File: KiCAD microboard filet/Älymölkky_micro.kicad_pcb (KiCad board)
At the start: 2 copper layers, 84 parts, among them U1 nRF52810-QCxx, X1 32MHz Crystal, X1_C1 12pF, X1_C2 12pF, X2 32.768 kHz Crystal, X2_C11 12pF, X2_C12 12pF

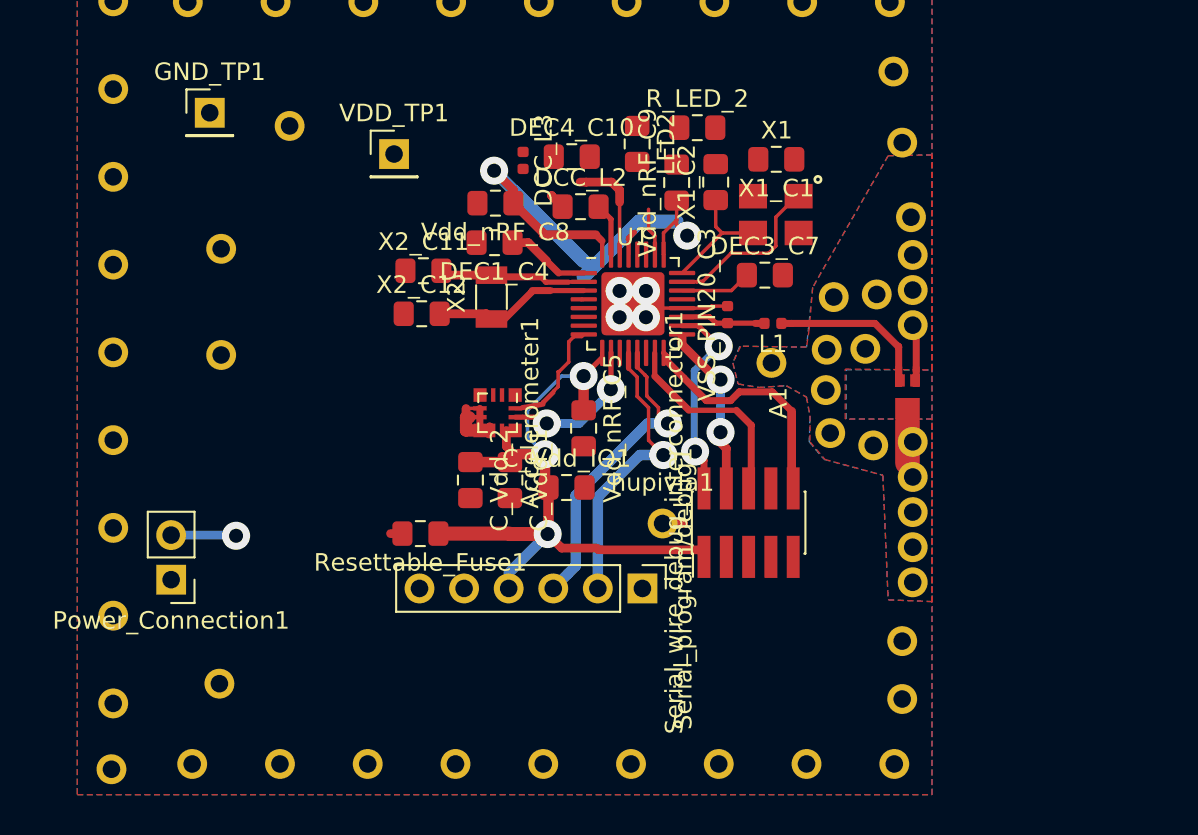
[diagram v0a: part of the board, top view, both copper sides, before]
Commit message: Changed programming interface to standalone pinheaders
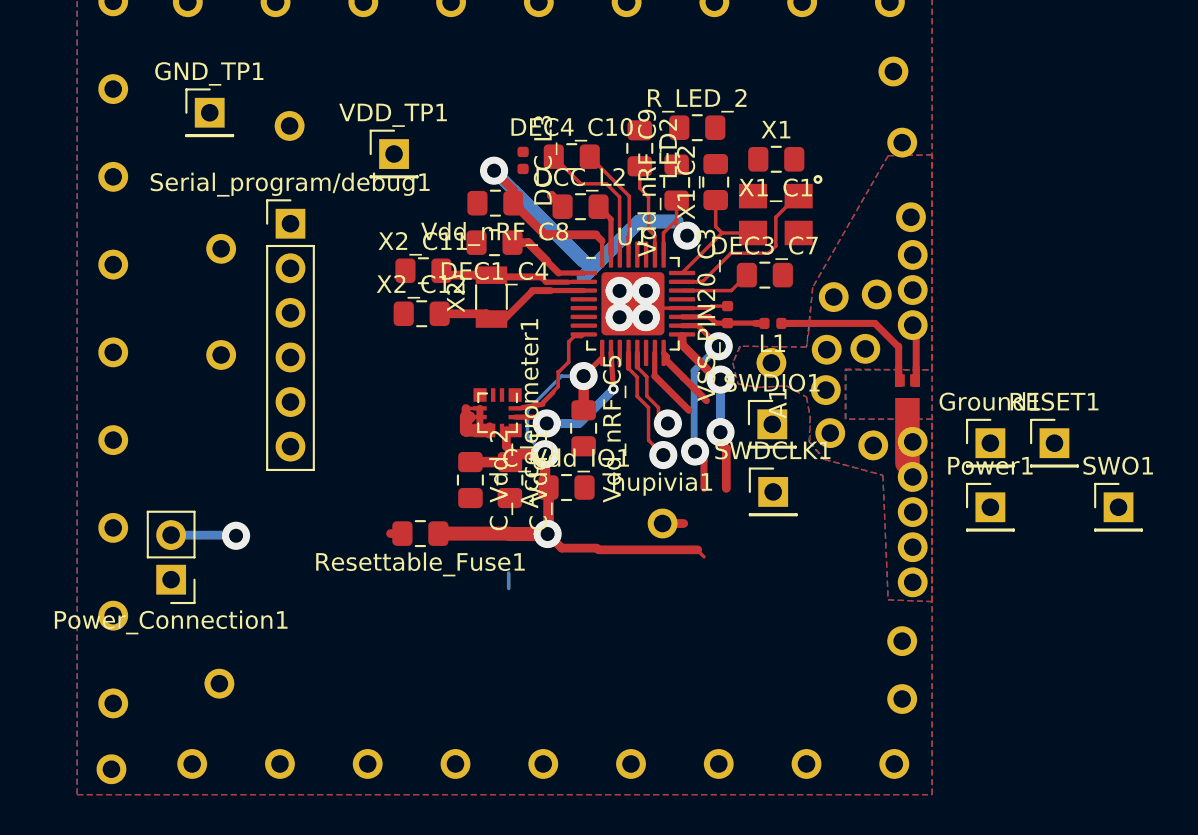
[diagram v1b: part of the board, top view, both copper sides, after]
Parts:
- removed Serial_wire_debug_interconnector1: Conn_02x05_Odd_Even, Connector_PinHeader_1.27mm:PinHeader_2x05_P1.27mm_Vertical_SMD
- added Ground1: Conn_01x01_Male, Connector_PinHeader_2.54mm:PinHeader_1x01_P2.54mm_Vertical, F.Cu at (151.2, 101.9)
- added Power1: Conn_01x01_Male, Connector_PinHeader_2.54mm:PinHeader_1x01_P2.54mm_Vertical, F.Cu at (151.2, 105.6)
- added RESET1: Conn_01x01_Male, Connector_PinHeader_2.54mm:PinHeader_1x01_P2.54mm_Vertical, F.Cu at (154.8, 101.9)
- added SWDCLK1: Conn_01x01_Male, Connector_PinHeader_2.54mm:PinHeader_1x01_P2.54mm_Vertical, F.Cu at (138.8, 104.7)
- added SWDIO1: Conn_01x01_Male, Connector_PinHeader_2.54mm:PinHeader_1x01_P2.54mm_Vertical, F.Cu at (138.8, 100.8)
- added SWO1: Conn_01x01_Male, Connector_PinHeader_2.54mm:PinHeader_1x01_P2.54mm_Vertical, F.Cu at (158.5, 105.6)
- moved Serial_program/debug1 28.9 mm to (111.3, 89.4), turned to 0 degrees
- moved LED2 0.29 mm to (131.2, 85.1)
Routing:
- net /~TX0: track 17.5 -> 4.74 mm
- net /~Reset: track 14.0 -> 4.01 mm
- net /~RX1: track 16.6 -> 6.65 mm
- net /~SWO: track 11.6 -> 4.08 mm
- net Earth: track 19.3 -> 24.5 mm
- net VDD: track 71.9 -> 68.8 mm
- net Net-(LED2-Pad2): track 2.73 -> 5.39 mm
- net Net-(DCC_L3-Pad1): track 6.12 -> 7.99 mm

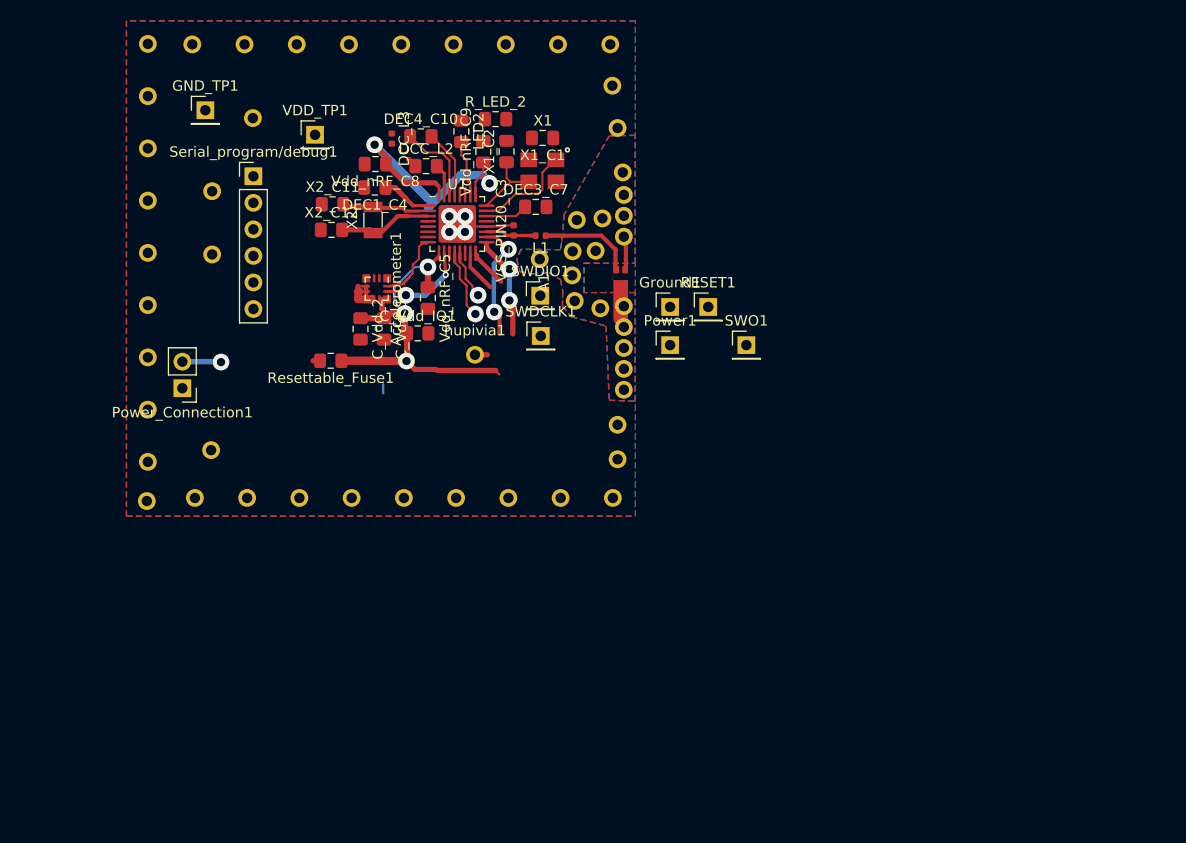
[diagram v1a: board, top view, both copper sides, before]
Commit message: Re-arranged most of the layout to more compact form, missing antennas
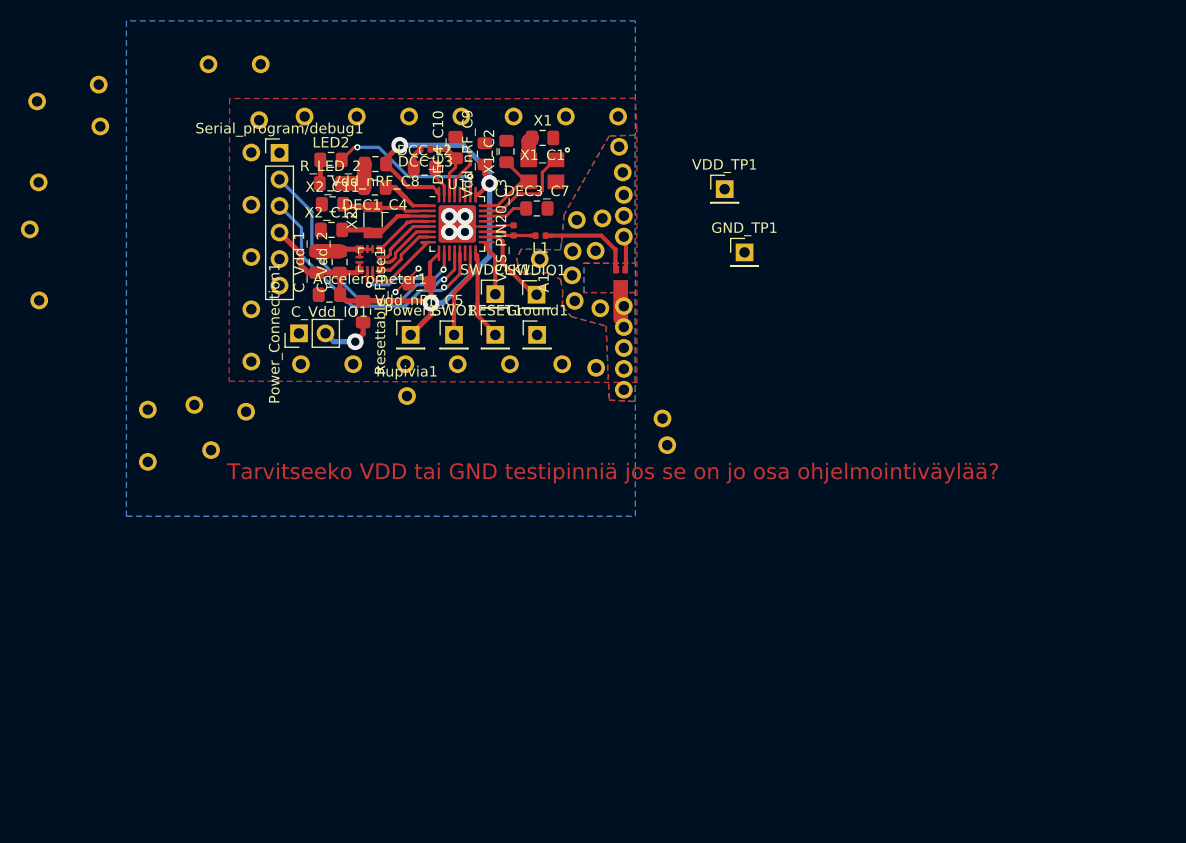
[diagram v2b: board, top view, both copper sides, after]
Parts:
- moved GND_TP1 53.4 mm to (158.3, 96.7)
- moved ? 49.2 mm to (96.7, 84.7)
- moved VDD_TP1 39.5 mm to (156.4, 90.7)
- moved SWO1 28.0 mm to (130.5, 104.6)
- moved Power1 24.8 mm to (126.3, 104.6)
- moved ? 21.8 mm to (90.8, 101.3)
- moved ? 20.7 mm to (90.6, 82.2)
- moved RESET1 20.5 mm to (134.4, 104.6)
- moved ? 17.6 mm to (89.9, 94.5)
- moved R_LED_2 17.0 mm to (118.7, 90.1)
- moved ? 16.6 mm to (90.8, 90.0)
- moved Ground1 13.0 mm to (138.4, 104.6)
- moved ? 12.9 mm to (111.8, 84.0)
- moved ? 12.8 mm to (140.8, 107.4)
- moved ? 12.8 mm to (135.8, 107.4)
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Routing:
- net /~TX0: track 4.74 -> 26.8 mm
- net /~RX1: track 6.65 -> 26.5 mm
- net Net-(LED2-Pad2): track 5.39 -> 15.7 mm, vias 0 -> 2
- net Earth: track 24.5 -> 31.1 mm, vias 4 -> 6
- net /~SCL_SPC: track 0.00 -> 6.10 mm
- net /~SAO_SDO: track 0.00 -> 6.03 mm
- net /~CS: track 0.00 -> 6.01 mm
- net /~SDA_SDI: track 0.16 -> 5.85 mm
- net /~SWDCLK: track 10.2 -> 5.54 mm, vias 2 -> 0
- net /~Reset: track 4.01 -> 8.61 mm
- net /~SWO: track 4.08 -> 8.47 mm
- net /~SWDIO: track 11.6 -> 8.34 mm, vias 2 -> 0
- net Net-(LED2-Pad1): track 0.00 -> 2.27 mm
- net /~INT2: track 9.73 -> 11.0 mm
- net Net-(DCC_L2-Pad1): track 0.91 -> 2.01 mm
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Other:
- board text added: "Tarvitseeko VDD tai GND testipinniä jos se on jo osa ohjelmointiväylää?"

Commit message: Changed serial programming pin locations and order, reorganized whole board
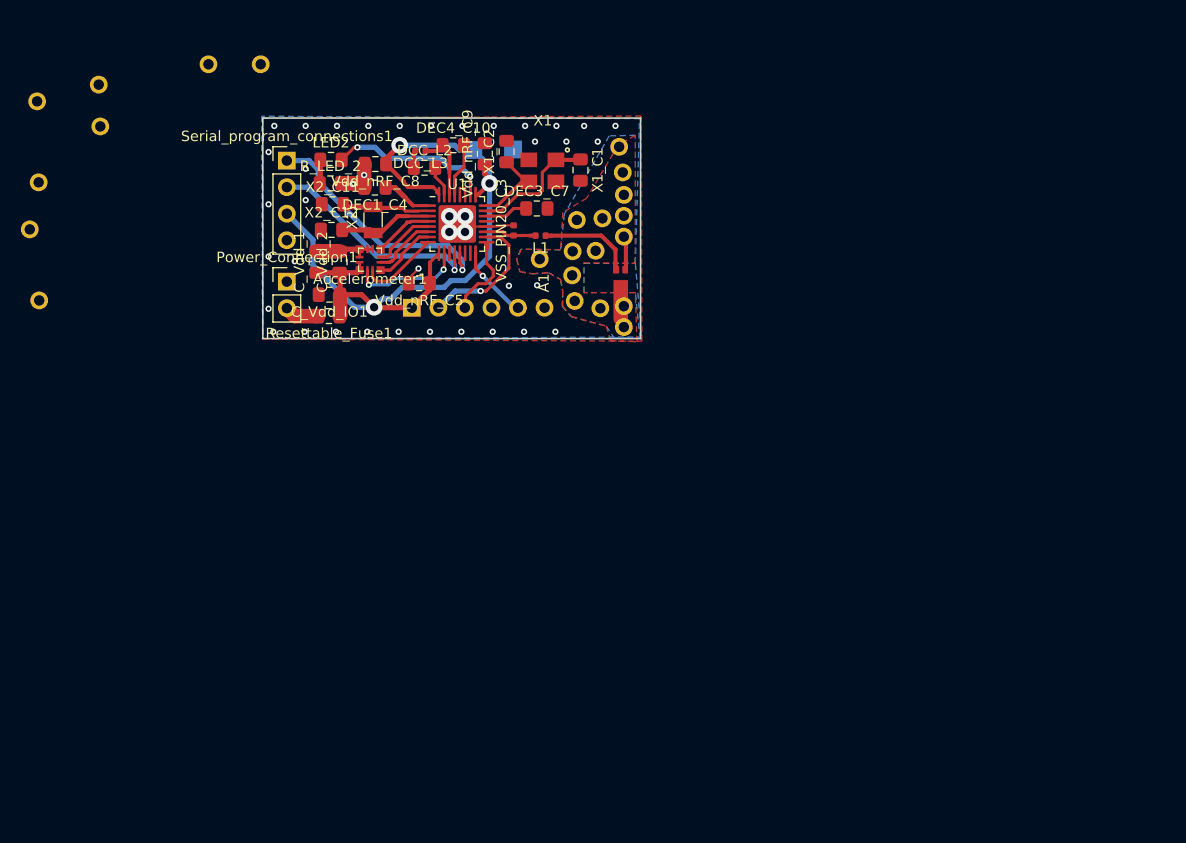
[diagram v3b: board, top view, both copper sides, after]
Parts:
- removed the ? at (111.8, 84.0)
- removed the ? at (111.1, 87.2)
- removed the ? at (111.1, 92.2)
- removed the ? at (111.1, 97.2)
- removed the ? at (111.1, 102.2)
- removed the ? at (111.1, 107.2)
- removed the ? at (101.2, 111.8)
- removed the ? at (101.2, 116.8)
- removed the ? at (107.2, 115.6)
- removed the ? at (150.9, 115.2)
- removed the ? at (144.1, 107.8)
- removed the ? at (140.8, 107.4)
- removed the ? at (135.8, 107.4)
- removed the ? at (130.8, 107.4)
- removed the ? at (125.8, 107.4)
- removed the ? at (126.2, 83.7)
- removed the ? at (120.8, 107.4)
- removed the ? at (115.8, 107.4)
- removed the ? at (110.6, 112.0)
- removed the ? at (105.7, 111.3)
- removed the ? at (146.8, 109.8)
- removed the ? at (146.8, 107.8)
- removed the ? at (146.8, 105.8)
- removed the ? at (141.2, 83.7)
- removed the ? at (150.4, 112.6)
- removed the ? at (116.2, 83.7)
- removed the ? at (121.2, 83.7)
- removed the ? at (136.2, 83.7)
- removed the ? at (146.2, 83.7)
- removed the ? at (131.2, 83.7)
- removed Ground1, Power1, RESET1, SWDCLK1, SWDIO1, SWO1, hupivia1: Conn_01x01_Male, Connector_PinHeader_2.54mm:PinHeader_1x01_P2.54mm_Vertical
- removed Serial_program/debug1: Conn_01x06_Male, Connector_PinHeader_2.54mm:PinHeader_1x06_P2.54mm_Vertical
- added SWD_connections1: Conn_01x06_Male, Connector_PinHeader_2.54mm:PinHeader_1x06_P2.54mm_Vertical, B.Cu at (126.5, 102.0)
- added Serial_program_connections1: Conn_01x04_Male, Connector_PinHeader_2.54mm:PinHeader_1x04_P2.54mm_Vertical, F.Cu at (114.5, 87.9)
- GND_TP1, VDD_TP1: moved to B.Cu
- moved VDD_TP1 24.3 mm to (132.3, 86.9)
- moved GND_TP1 24.2 mm to (136.2, 86.8)
- moved Power_Connection1 5.08 mm to (114.5, 99.5), turned to 0 degrees
- moved X1_C1 4.75 mm to (142.6, 88.8), turned to 270 degrees
- moved Resettable_Fuse1 3.30 mm to (118.5, 102.8), turned to 180 degrees
- moved DCC_L3 0.50 mm to (127.3, 87.0)
- moved DEC4_C10 0.32 mm to (130.4, 86.5), turned to 0 degrees
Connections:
- U1 pad 15: /~SWO -> Net-(U1-Pad15)
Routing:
- net VDD: track 68.9 -> 80.3 mm
- net /~SWO: track 8.47 -> 0.00 mm
- net /~RX1: track 26.5 -> 21.2 mm
- net /~SWDIO: track 8.34 -> 13.0 mm, vias 0 -> 1
- net /~SWDCLK: track 5.54 -> 8.33 mm
- net Earth: track 31.1 -> 28.5 mm, vias 6 -> 41
- net Net-(U1-Pad23): track 9.67 -> 12.0 mm
- net Net-(Power_Connection1-Pad2): track 5.34 -> 3.31 mm, vias 1 -> 0
- net /~Reset: track 8.61 -> 7.11 mm, vias 0 -> 1
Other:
- board outline added: 36.1 x 21.1 mm
- board text removed: "Tarvitseeko VDD tai GND testipinniä jos se on jo osa ohjelmointiväylää?"

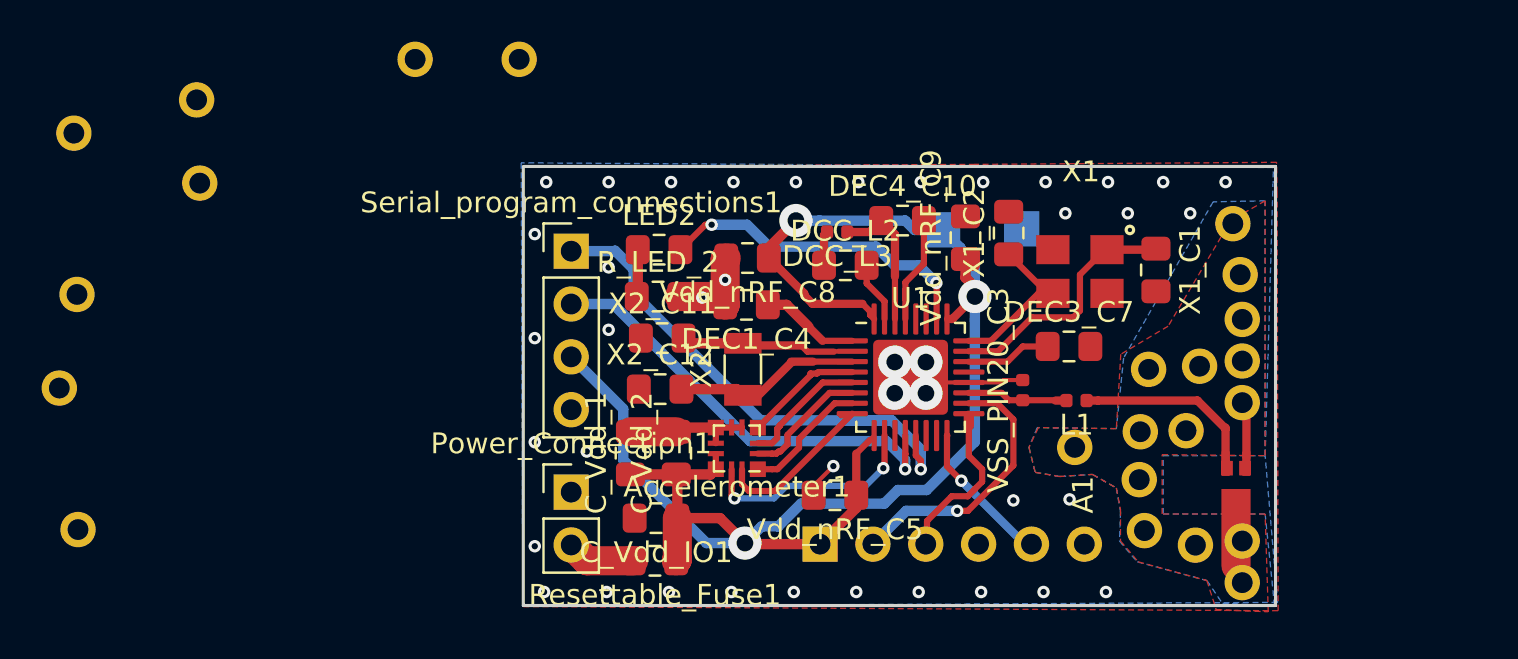
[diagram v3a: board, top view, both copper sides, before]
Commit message: Changed all vias to smaller size, passed electronic rule check
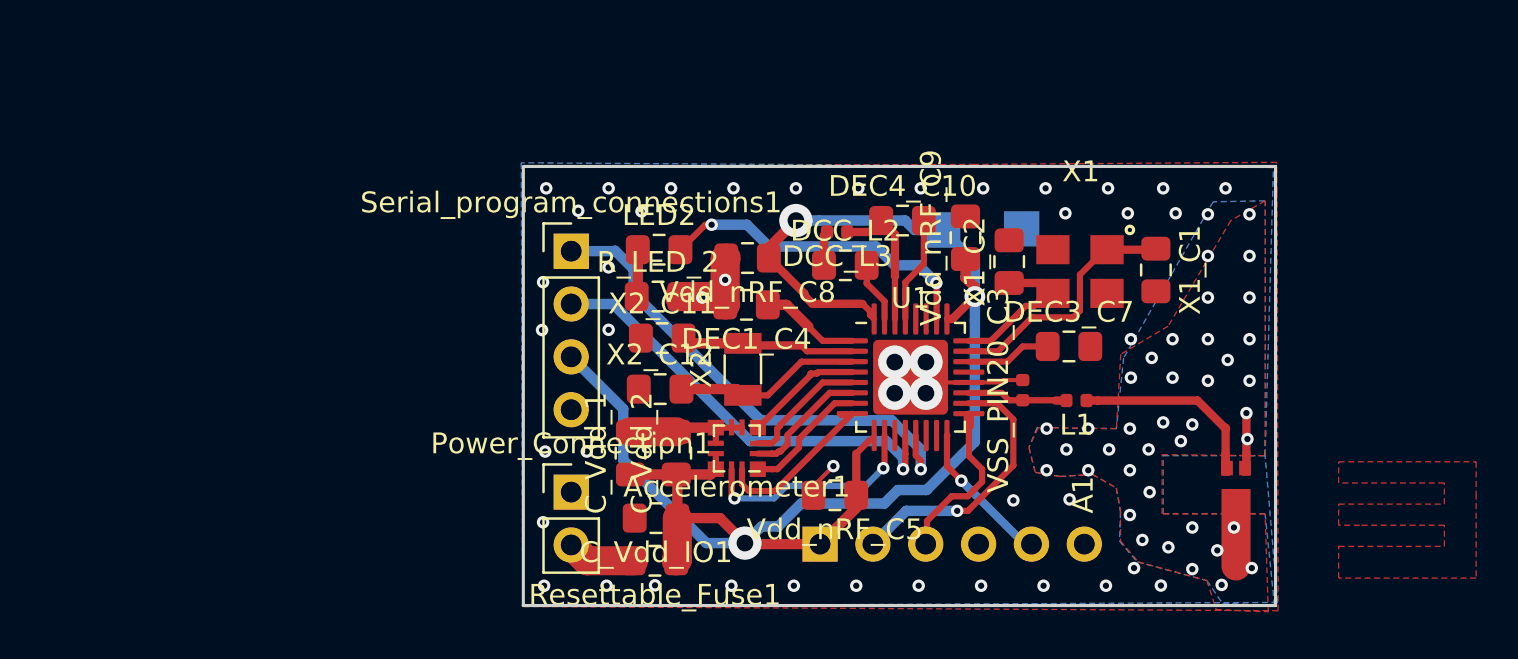
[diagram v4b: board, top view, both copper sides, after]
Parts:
- removed ? (x23): Conn_01x01_Male, Connector_PinHeader_2.54mm:PinHeader_1x01_P2.54mm_Vertical
- moved X1_C2 1.38 mm to (135.6, 88.4)
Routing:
- net Net-(U1-Pad3): track 8.83 -> 9.41 mm
- net Earth: vias 41 -> 85
- added copper zone on F.Cu, net (none)
